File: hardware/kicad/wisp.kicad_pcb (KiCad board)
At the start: 2 copper layers, 100 x 100 mm, 73 parts, among them J1 USB-C, J2 Second I2C Bus, J3 mmWave UART (LD2410), J4 I2S Mic (INMP441), J5 Switched DC Output, J6 Reed/Hall Contact, J7 1-Wire Bus, J8 Analog Sensor Pad, J9 Expansion Header, Q1 MMBT3904, Q2 MMBT3904, Q3 2N7002, Q4 MMBT3904, SW1 RESET, SW2 BOOT, U1 CH340C, U2 AP63203WU-7, U3 ESP32-WROOM-32, U4 SCD41-D-R2, U5 BME680, U6 BH1750FVI-TR

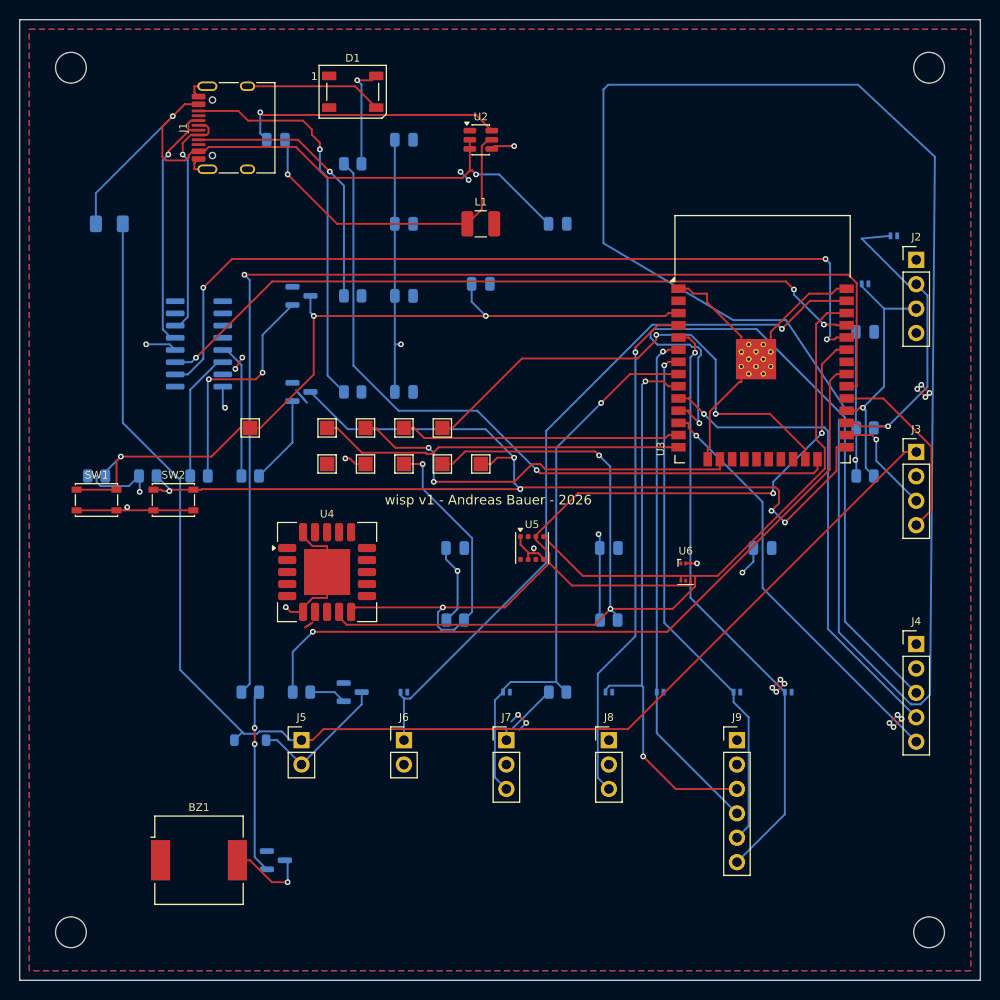
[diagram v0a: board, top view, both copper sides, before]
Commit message: Rebuild PCB as 4-layer with a functional floorplan; DRC fully clean
The long-running "unconnected GND/+3V3 pour island" problem (#8) was not a
routing problem. Three passes tried to stitch the islands shut; this
replaces the layout that produced them.

Root causes found:

- 2-layer stackup where B.Cu was both the ground plane and a routing
  layer. ~1.4m of signal traces plus 40 backside parts shredded it, and
  +3V3 was a second pour competing for F.Cu. Neither power net had a
  reliable path to every pad.
- Every decoupling capacitor sat on the opposite copper layer, 8-20mm
  from the pin it served (C11 for the ESP32: 11.3mm). The five pads that
  defeated every stitching attempt were exactly the U5/U6 power pins.
  A 12-waypoint stitch around a board quadrant is not a bypass return.
- Placement had been produced by proportionally scaling an older, denser
  board, so growing the board never changed the pin-level geometry that
  actually blocked routing.
- U3's courtyard was stale: written in absolute board coordinates into
  the footprint's local space, so it never moved with the module. The
  MH1/MH2/J1-vs-U3 overlaps previously recorded as "DRC engine noise,
  geometrically impossible" were real; that check had compared footprint
  origins rather than courtyard geometry.

Changes:

- 4-layer stackup: In1.Cu a solid GND plane, In2.Cu a solid +3V3 plane,
  nothing routed on either. The DSN is patched to mark them (type power)
  so the autorouter cannot cut them.
- Every +3V3/GND pad bonded to its plane by its own stub and via (107
  pads, plus ~195 GND stitching vias). A power pad can now only be
  unconnected if its via is missing, which DRC reports directly.
- Board 100x100mm -> 60x80mm, re-floorplanned by function: ESP32 at the
  top edge with the antenna off-board, decoupling within 1.8-3.0mm of its
  pin on the same side, tight buck loop, connectors on edges.
- All 73 parts on the front: single-sided assembly.
- Sensors on a thermally isolated tab, cut free b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
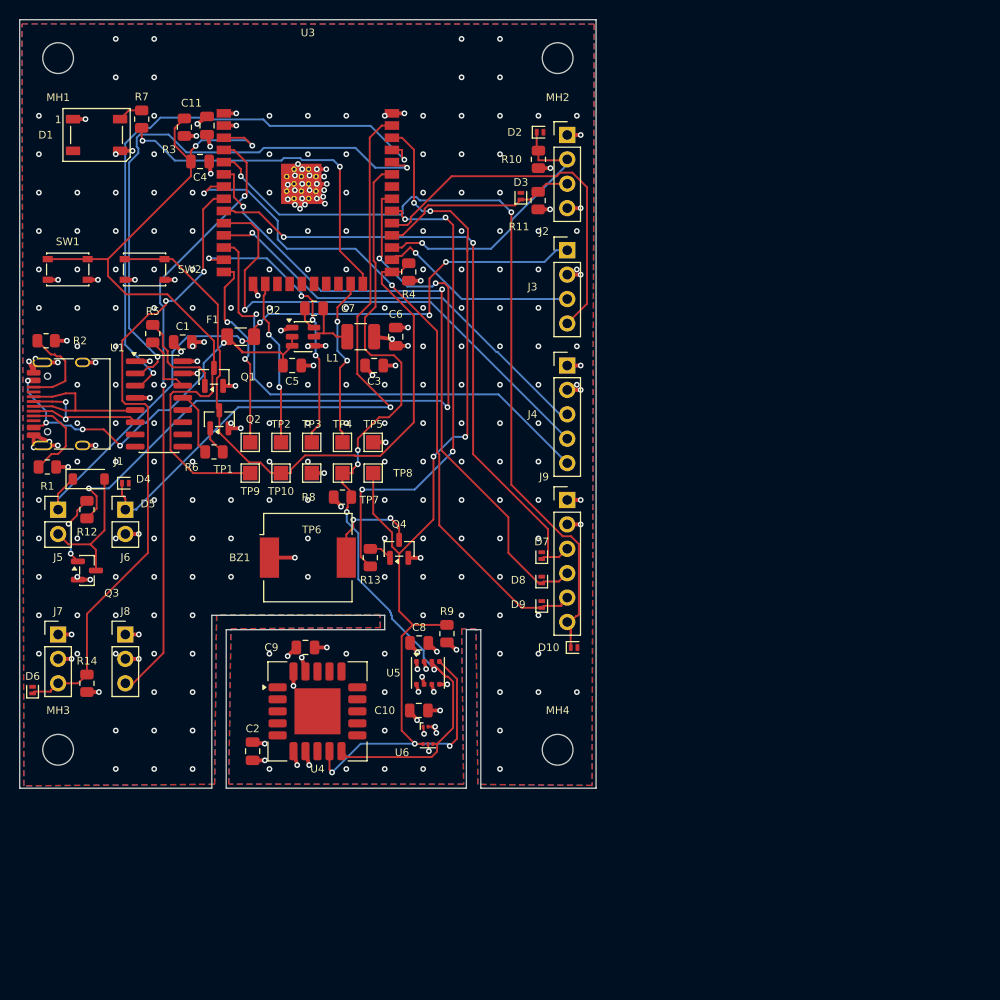
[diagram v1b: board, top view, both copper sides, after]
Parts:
- C1, C10, C11, C2, C3, C4, C5, C6, C7, C8, C9, D10, D2, D3, D4, D5, D6, D7, D8, D9, F1, Q1, Q2, Q3, Q4, R1, R10, R11, R12, R13, R14, R2, R3, R4, R5, R6, R7, R8, R9, U1: moved to F.Cu
- moved C11 71.8 mm to (19.5, 11.0), turned to 90 degrees
- moved J8 51.5 mm to (11.0, 64.0)
- moved U3 50.7 mm to (30.0, 18.0)
- moved D6 49.3 mm to (1.34, 69.8), turned to 90 degrees
- moved R14 49.0 mm to (7.00, 69.1), turned to 90 degrees
- moved J7 47.9 mm to (4.00, 64.0)
- moved J4 46.5 mm to (57.0, 36.0)
- moved R11 44.5 mm to (54.0, 18.8), turned to 90 degrees
- moved R10 44.0 mm to (54.0, 14.5), turned to 90 degrees
- moved MH4 43.1 mm to (56.0, 76.0)
- moved J3 42.0 mm to (57.0, 24.0)
- moved C2 40.6 mm to (24.2, 76.2), turned to 90 degrees
- moved C10 39.6 mm to (41.5, 71.9)
- moved MH2 38.7 mm to (56.0, 4.00)
- moved J2 38.6 mm to (57.0, 12.0)
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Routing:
- net GND: track 291.6 -> 87.6 mm, vias 22 -> 266
- net /BUZZER_CTRL: track 119.9 -> 50.6 mm, vias 1 -> 4
- net /+5V_EXT: track 142.4 -> 74.0 mm, vias 0 -> 4
- net /IO0: track 114.4 -> 70.1 mm, vias 5 -> 0
- net +3V3: track 86.2 -> 45.6 mm, vias 10 -> 35
- net /LED_CTRL: track 75.6 -> 36.5 mm, vias 1 -> 2
- net /JTAG_TDO: track 51.4 -> 17.9 mm
- net /CC2: track 41.3 -> 9.29 mm, vias 1 -> 0
- net /MIC_WS: track 72.9 -> 43.7 mm
- net /BUCK_SW: track 34.6 -> 6.38 mm, vias 1 -> 0
- net /CH_TXD: track 87.9 -> 59.8 mm, vias 3 -> 2
- net +5V: track 70.6 -> 43.5 mm, vias 2 -> 5
- net /JTAG_TCK: track 43.0 -> 17.3 mm
- net /BUCK_BST: track 28.0 -> 2.50 mm, vias 1 -> 0
- net /SDA: track 113.8 -> 88.9 mm
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- added copper zone on In2.Cu, net +3V3
- added copper zone on F.Cu, net GND
- added copper zone on In1.Cu, net GND
- removed copper zone on F.Cu, net +3V3
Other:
- board size 100 x 100 mm -> 60 x 80 mm
- copper layers 2 -> 4

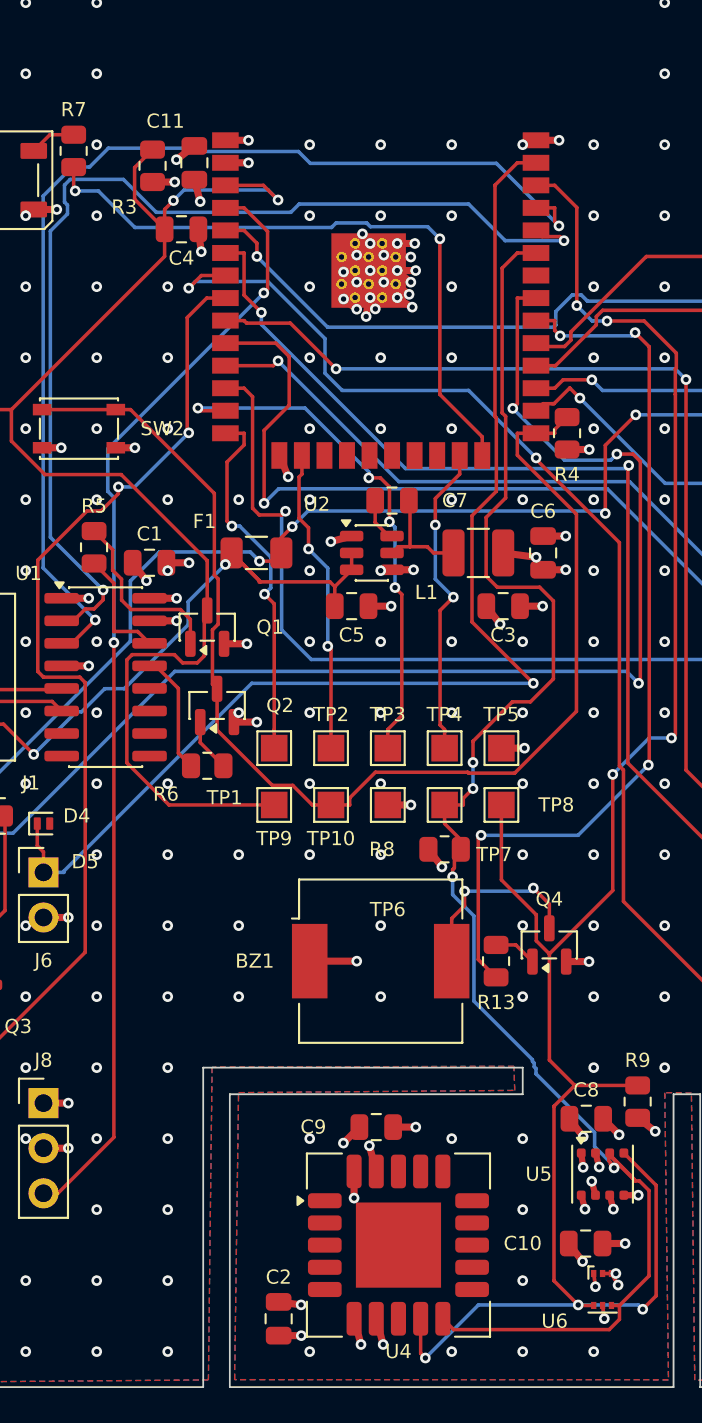
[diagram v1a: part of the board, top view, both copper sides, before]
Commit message: Give the ESP32 a populated bypass cap (C11 is DNP)
The placement pass assigned C11 to U3 as its 100nF bypass, but C11 is
flagged DNP in the schematic -- it belongs to the optional expansion
block. The board would therefore have shipped with no populated local
decoupling on the ESP32, while the SCD41 got two caps. That is the exact
defect class this rework set out to fix, so it is worth catching here.

Swapped the positions of C2 (populated) and C11 (DNP). Both are
C_0805_2012Metric with identical pad nets and the same rotation, so this
is a pure relabel: no copper changes, and the existing plane-bonding
stubs and vias serve the swapped pads unchanged.

  C2 -> U3 pin 2 (+3V3):  1.99mm, populated
  C9 -> U4 pin 19 (+3V3): 2.67mm, populated  (unchanged)

Populated 100nF caps now map one-per-IC: C1->U1, C2->U3, C8->U5,
C9->U4, C10->U6.

DRC re-verified: 0 violations, 0 unconnected. Gerbers/drill/CPL
re-exported; BOM unchanged.

Co-Authored-By: Claude Opus 5 <noreply@anthropic.com>
Claude-Session: https://claude.ai/code/session_01E96k4vTKDQq4v628HKK7gR
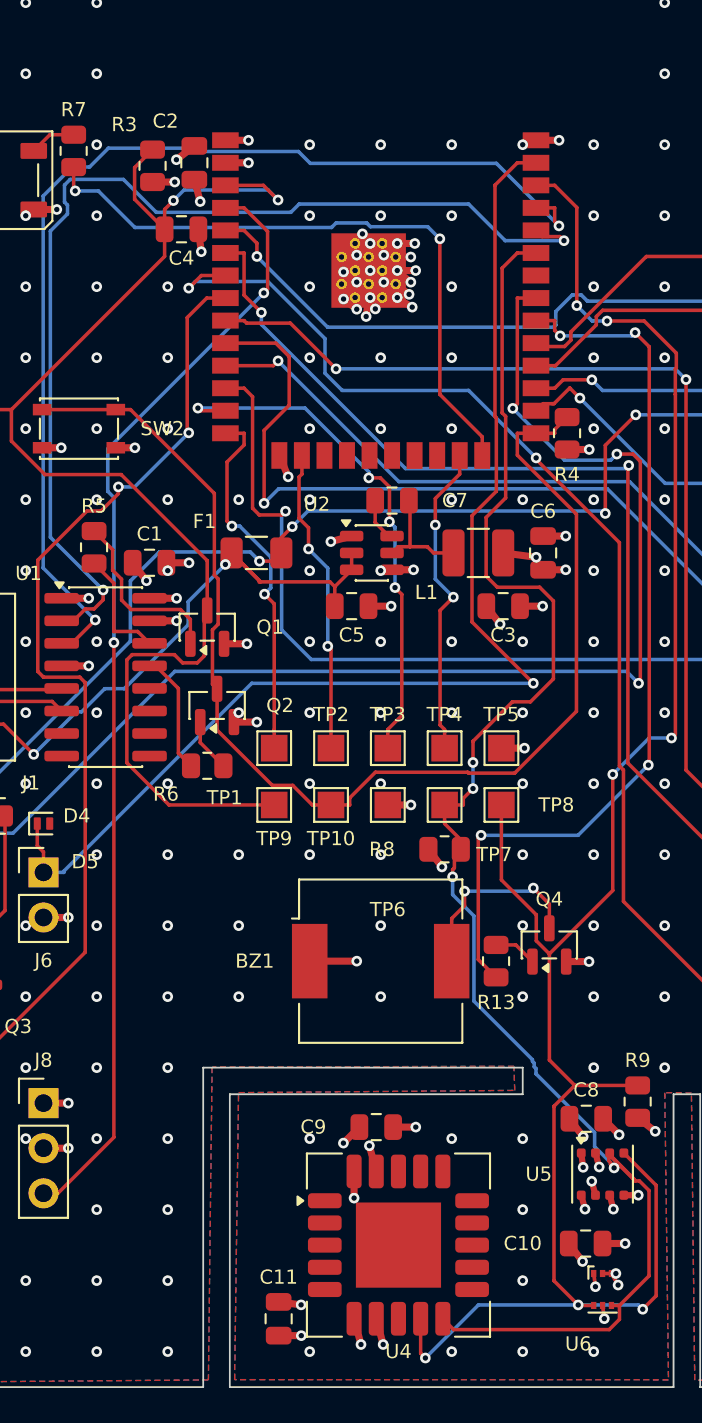
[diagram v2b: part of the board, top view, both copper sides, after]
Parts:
- moved C11 65.3 mm to (24.2, 76.2)
- moved C2 65.3 mm to (19.5, 11.0)
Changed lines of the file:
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@@
 	(footprint "C_0805_2012Metric"
 		(layer "F.Cu")
-		(at 24.25 76.15 90)
+		(at 19.5 11.02 90)
 		(descr "Capacitor SMD 0805 (2012 Metric), square (rectangular) end terminal, IPC-7351 nominal, (Body size source: IPC-SM-782 page 76, https://www.pcb-3d.com/wordpress/wp-content/uploads/ipc-sm-782a_amendment_1_and_2.pdf, https://docs.google.com/spreadsheets/d/1BsfQQcO9C6DZCsRaXUlFlo91Tg2WpOkGARC1WS5S8t0/edit?usp=sharing)")
 		(tags "capacitor")
 		(property "Reference" "C2"
-			(at 2.345 0 0)
+			(at 2.345 -1.625 0)
 			(layer "F.SilkS")
 			(effects
@@
 	(footprint "C_0805_2012Metric"
 		(layer "F.Cu")
-		(at 19.5 11.02 90)
+		(at 24.25 76.15 90)
 		(descr "Capacitor SMD 0805 (2012 Metric), square (rectangular) end terminal, IPC-7351 nominal, (Body size source: IPC-SM-782 page 76, https://www.pcb-3d.com/wordpress/wp-content/uploads/ipc-sm-782a_amendment_1_and_2.pdf, https://docs.google.com/spreadsheets/d/1BsfQQcO9C6DZCsRaXUlFlo91Tg2WpOkGARC1WS5S8t0/edit?usp=sharing)")
 		(tags "capacitor")
 		(property "Reference" "C11"
-			(at 2.345 -1.625 0)
+			(at 2.345 0 0)
 			(layer "F.SilkS")
 			(effects
@@
 		(tags "BH1750 WSOF6 ambient light sensor DRAFT-VERIFY")
 		(property "Reference" "U6"
-			(at -2.7 1.78685 0)
+			(at -1.37 3.06545 0)
 			(layer "F.SilkS")
 			(effects
@@
 		(tags "resistor")
 		(property "Reference" "R3"
-			(at -2.325 -1.595 0)
+			(at 2.325 -1.595 0)
 			(layer "F.SilkS")
 			(effects
